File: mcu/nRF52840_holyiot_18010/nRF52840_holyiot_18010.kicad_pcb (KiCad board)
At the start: 2 copper layers, 2 parts

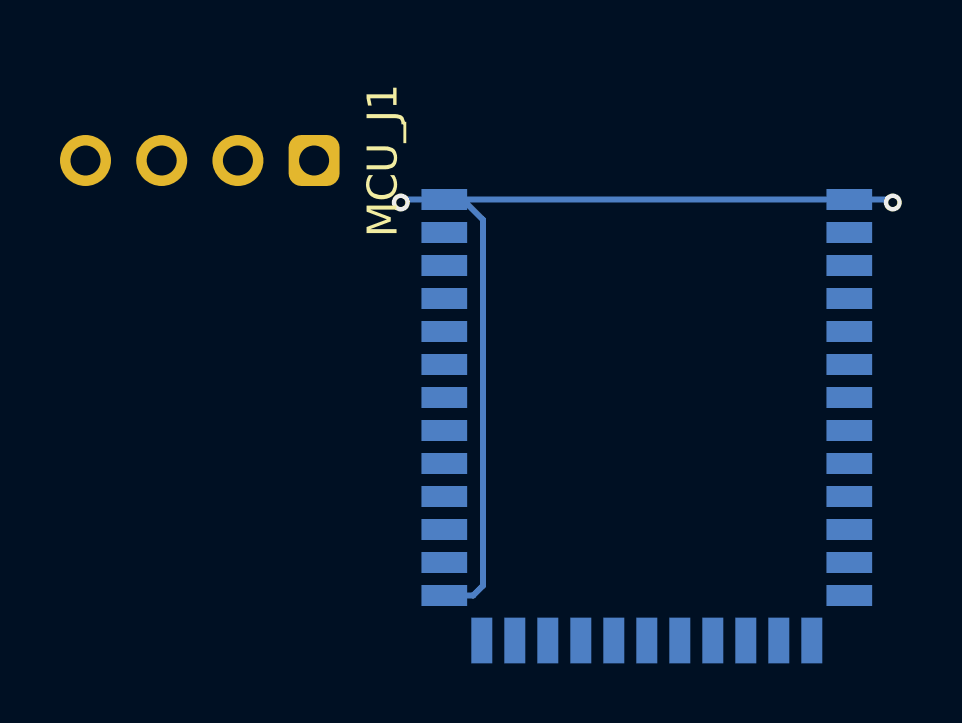
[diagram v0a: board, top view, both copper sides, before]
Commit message: add SWC SWD track in mcu
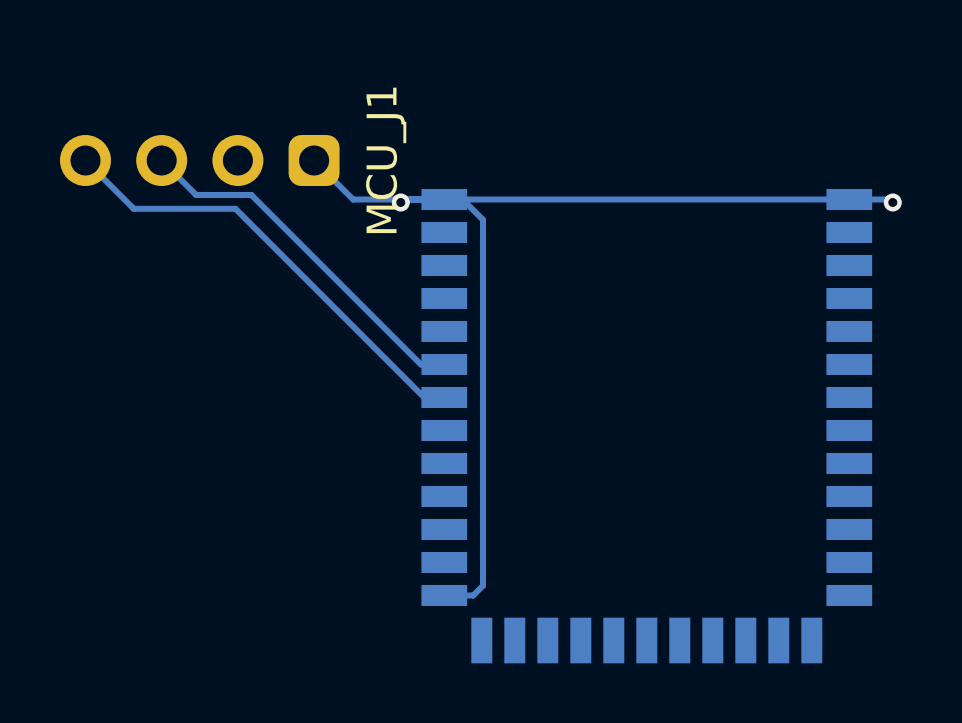
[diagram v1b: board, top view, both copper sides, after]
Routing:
- net SWC: track 0.00 -> 15.2 mm
- net SWD: track 0.00 -> 12.2 mm
- net GND: track 31.7 -> 36.6 mm
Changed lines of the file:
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@@
 		)
+	)
+	(segment
+		(start -7.53 -0.2)
+		(end -6.75 -0.2)
+		(width 0.2)
+		(layer "B.Cu")
+		(net 1)
+	)
+	(segment
+		(start -13.18 -5.85)
+		(end -7.53 -0.2)
+		(width 0.2)
+		(layer "B.Cu")
+		(net 1)
+	)
+	(segment
+		(start -15.02 -5.85)
+		(end -13.18 -5.85)
+		(width 0.2)
+		(layer "B.Cu")
+		(net 1)
+	)
+	(segment
+		(start -16.17 -7)
+		(end -15.02 -5.85)
+		(width 0.2)
+		(layer "B.Cu")
+		(net 1)
 	)
 	(via
@@
 		(start 6.75 -5.7)
 		(end 8.1 -5.7)
+		(width 0.2)
+		(layer "B.Cu")
+		(net 3)
+	)
+	(segment
+		(start -11.09 -7)
+		(end -9.79 -5.7)
 		(width 0.2)
 		(layer "B.Cu")
@@
 		(net 3)
 	)
+	(segment
+		(start -9.79 -5.7)
+		(end -6.75 -5.7)
+		(width 0.2)
+		(layer "B.Cu")
+		(net 3)
+	)
+	(segment
+		(start -17.135 -5.425)
+		(end -17.1 -5.39)
+		(width 0.2)
+		(layer "B.Cu")
+		(net 4)
+	)
+	(segment
+		(start -7.42 0.9)
+		(end -6.75 0.9)
+		(width 0.2)
+		(layer "B.Cu")
+		(net 4)
+	)
+	(segment
+		(start -17.1 -5.39)
+		(end -13.71 -5.39)
+		(width 0.2)
+		(layer "B.Cu")
+		(net 4)
+	)
+	(segment
+		(start -13.71 -5.39)
+		(end -7.42 0.9)
+		(width 0.2)
+		(layer "B.Cu")
+		(net 4)
+	)
+	(segment
+		(start -18.71 -7)
+		(end -17.135 -5.425)
+		(width 0.2)
+		(layer "B.Cu")
+		(net 4)
+	)
 	(embedded_fonts no)
